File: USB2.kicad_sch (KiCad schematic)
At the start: 0 parts

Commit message: usb work cont
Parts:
- added P1: USB_C_Plug_USB2.0, symbol Connector:USB_C_Plug_USB2.0
- added U2: TUSB2046BIVFR, TUSB2046BIVFR:QFP80P900X900X145-32N, symbol TUSB2046BIVFR:TUSB2046BIVFR
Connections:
- new net: P1.A1 (GND), P1.A12 (GND), P1.B1 (GND), P1.B12 (GND)
- new net: P1.A4 (VBUS), P1.A9 (VBUS), P1.B4 (VBUS), P1.B9 (VBUS)
- new net USB2_HOST2_DM: U2.2 (DM0)
- new net USB2_HOST2_DP: U2.1 (DP0)

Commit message: usb work cont
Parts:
- added C1, C2: 100uF, symbol Device:C_Polarized
- added C3, C4: 0.1uF/16V, symbol Device:C_Polarized
- added C5: 10uF/10V, symbol Device:C_Polarized
- added C6: 22uF/10V, symbol Device:C_Polarized
- added C7: 1uF/10V, symbol Device:C_Polarized
- added P2: USB_C_Plug_USB2.0, symbol Connector:USB_C_Plug_USB2.0
- added R1: 4.7k/1%, symbol Device:R
- added R2: 120K, symbol Device:R
- added U3: TPS2044BDR, TPS2044BDR:SOIC127P600X175-16N, symbol TPS2044BDR:TPS2044BDR
- added U4: ~, symbol raxda:SGM2576YN5G/TR
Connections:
- net GND: now reaches P1.A1 (GND), P1.A12 (GND), P1.B1 (GND), P1.B12 (GND)
- net GND: now also P1.S1 (SHIELD), C1.2, C2.2, C3.2, C4.2, C5.2, C6.2, C7.2, P2.A1 (GND), P2.A12 (GND), P2.B1 (GND), P2.B12 (GND), P2.S1 (SHIELD), R1.2, R2.2, U3.1 (GND), U3.5 (GND__1), U4.2 (GND)
- net at P1.A4 (VBUS), P1.A9 (VBUS), P1.B4 (VBUS)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: now also C2.1, U3.14 (OUT2)
- net at P1.A6 (D+): now also U2.16 (DP2)
- net at P1.A7 (D-): now also U2.15 (DM2)
- net at U2.10 (~OVRCUR1): now also U3.16 (~{OC1})
- net at U2.11 (DM1): now also P2.A7 (D-)
- net at U2.12 (DP1): now also P2.A6 (D+)
- net at U2.13 (~PWRON2): now also U3.4 (~{EN2})
- net at U2.14 (~OVRCUR2): now also U3.13 (~{OC2})
- net at U2.9 (~PWRON1): now also U3.3 (~{EN1})
- new net: C1.1, P2.A4 (VBUS), P2.A9 (VBUS), P2.B4 (VBUS), P2.B9 (VBUS), U3.15 (OUT1)
- new net: C3.1, C4.1, C5.1, C6.1, U3.2 (IN1), U3.6 (IN2), U4.1 (VOUT)
- new net: R1.1, U4.3 (OCB)
- new net Camera_GPIO: R2.1, U4.4 (EN)
- new net VCC5V0_USB: C7.1, U4.5 (IN)
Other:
- moved on the sheet: P1

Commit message: usb work cont
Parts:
- added C8: 10uF/10V, symbol Device:C_Polarized
- added C9: 10uF/X5R, symbol Device:C_Polarized
- added R3: 100K, symbol Device:R
- added R4: 3.9K, symbol Device:R
- added R5: 10K, symbol Device:R
- added U5: ~, symbol raxda:SGM2576YN5G/TR
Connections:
- net GND: now also C8.2, R3.2, R4.2, U5.2 (GND)
- net Switched 3.3v: now reaches U2.26 (~EXTMEM)
- net Switched 3.3v: now also C9.1, U5.1 (VOUT)
- new net: R4.1, U5.3 (OCB)
- new net: R3.1, R5.1, U5.4 (EN)
- new net +1.8v_(Output): R5.2
- new net +3.3v_(Output): C8.1, U5.5 (IN)

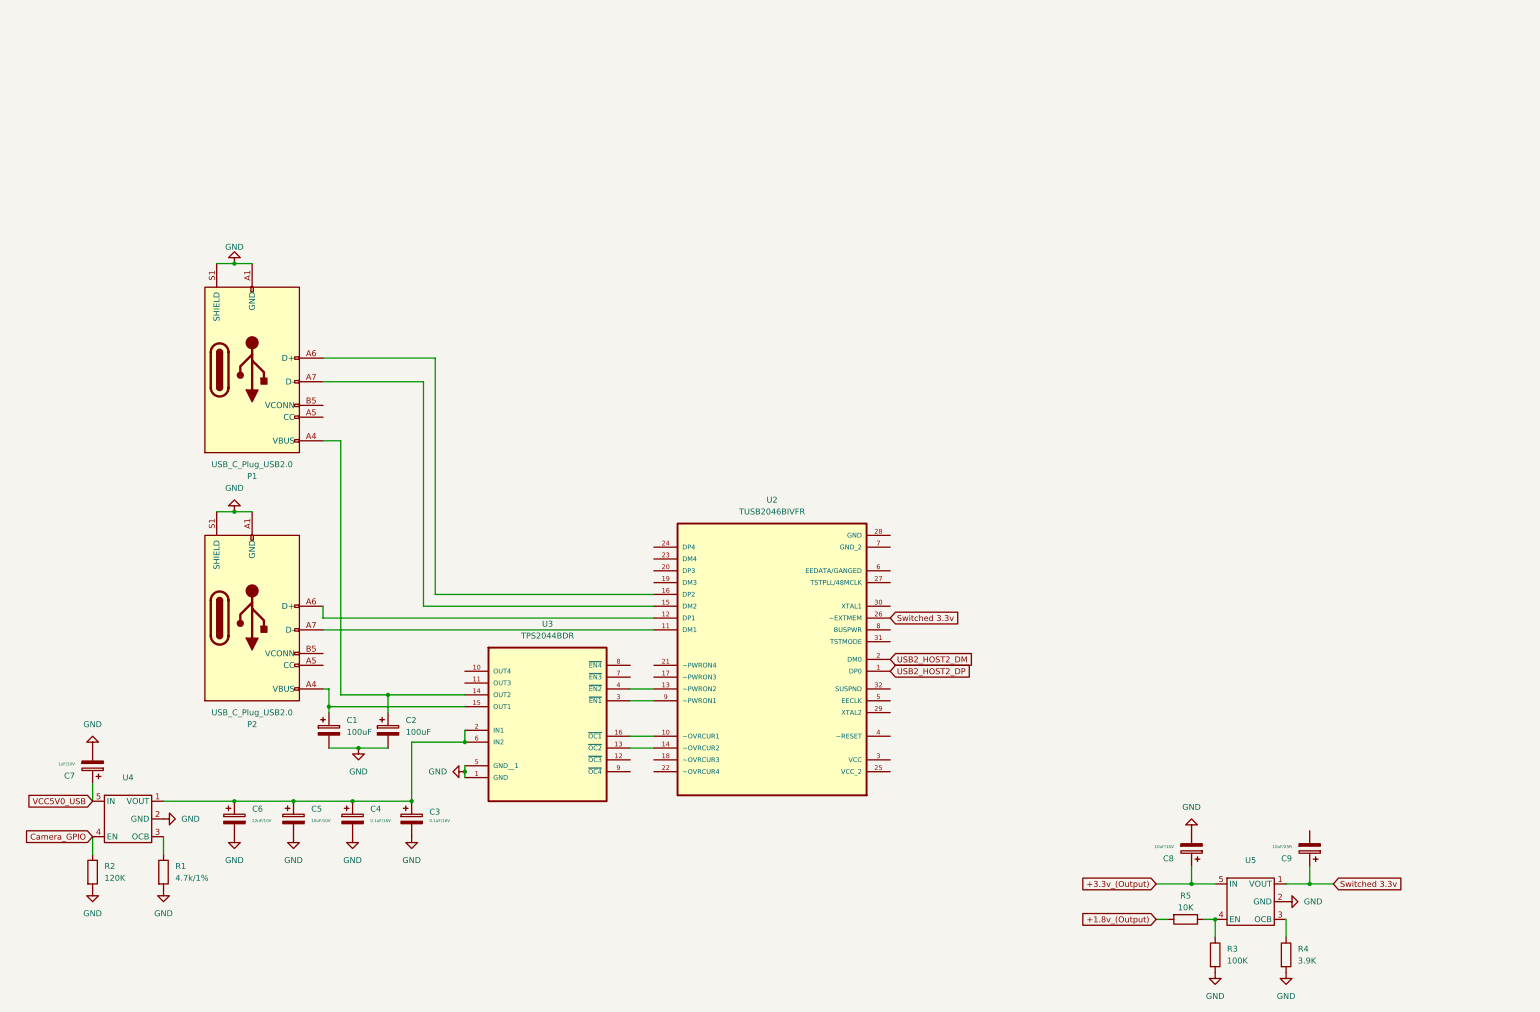
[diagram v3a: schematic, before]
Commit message: finished USB 2.0
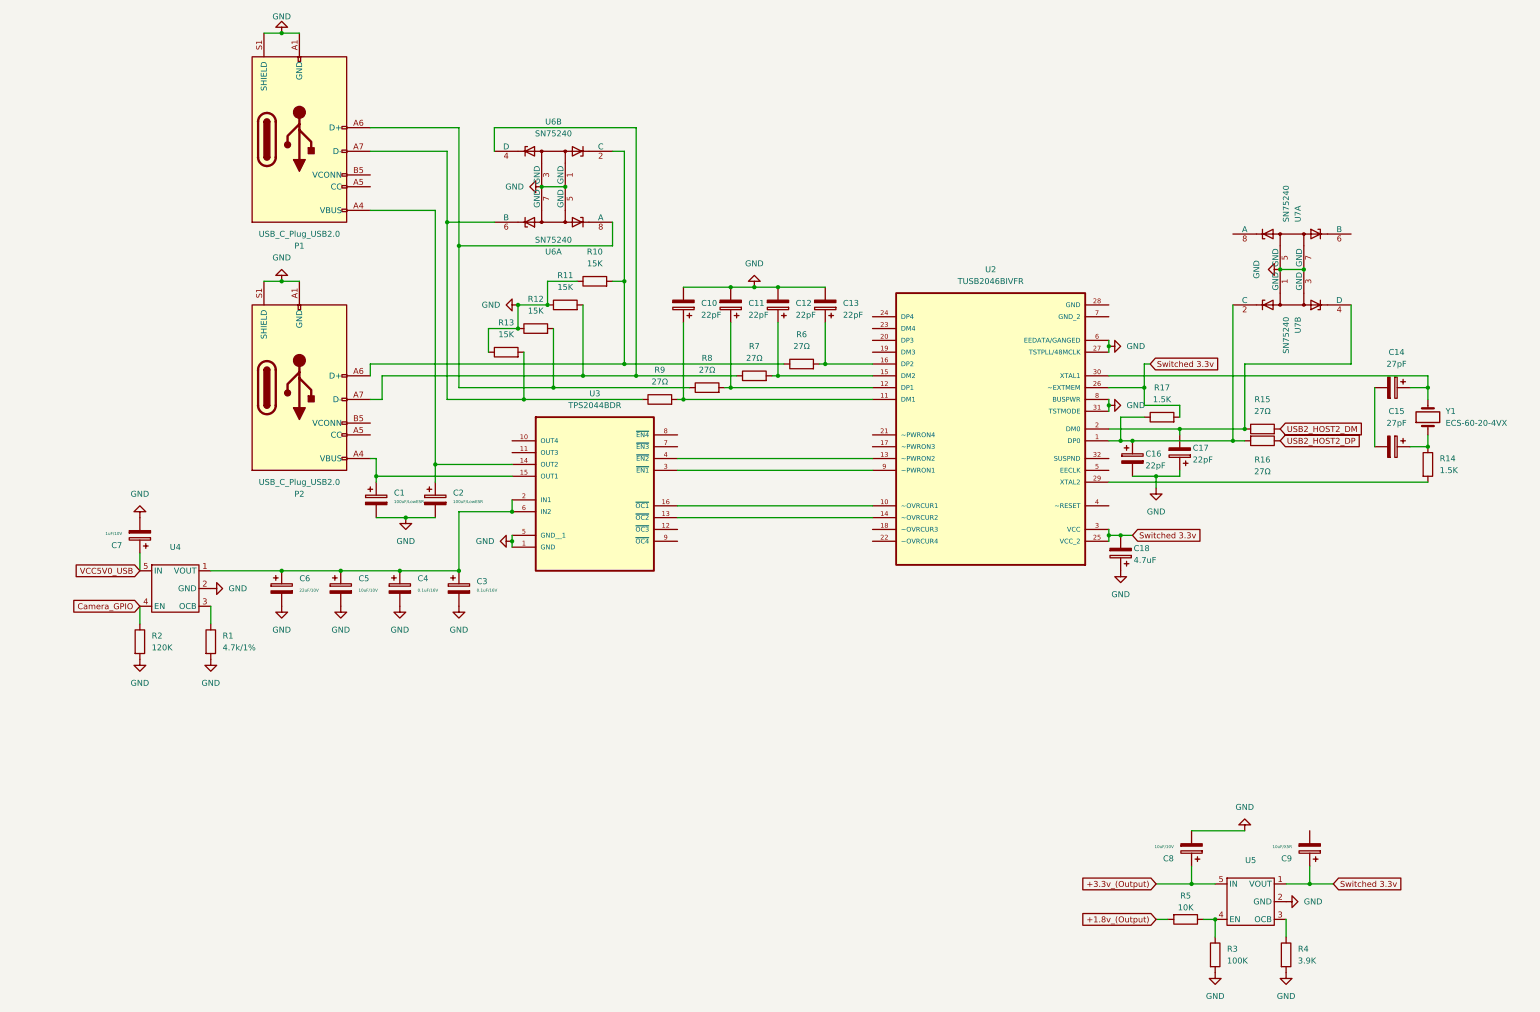
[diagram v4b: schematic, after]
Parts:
- added C10, C11, C12, C13, C16, C17: 22pF, symbol Device:C_Polarized
- added C14, C15: 27pF, symbol Device:C_Polarized
- added C18: 4.7uF, symbol Device:C_Polarized
- added R10, R11, R12, R13: 15K, symbol Device:R
- added R14, R17: 1.5K, symbol Device:R
- added R15, R16, R6, R7, R8, R9: 27Ω, symbol Device:R
- added U6, U7: SN75240, symbol Power_Protection:SN75240
- added Y1: ECS-60-20-4VX, symbol Device:Crystal
- C1, C2: value 100uF -> 100uF/LowESR
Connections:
- net GND: now also U2.27 (TSTPLL/48MCLK), U2.31 (TSTMODE), U2.6 (EEDATA/GANGED), U2.8 (BUSPWR), C10.2, C11.2, C12.2, C13.2, C16.2, C17.1, C18.1, R10.1, R11.1, R12.1, R13.1, U6.1 (GND), U6.3 (GND), U6.5 (GND), U6.7 (GND), U7.1 (GND), U7.3 (GND), U7.5 (GND), U7.7 (GND)
- net Switched 3.3v: now also U2.25 (VCC_2), U2.3 (VCC), C18.2, R17.2
- net USB2_HOST2_DM: now also R15.2; no longer U2.2 (DM0)
- net USB2_HOST2_DP: now also R16.1; no longer U2.1 (DP0)
- net at P1.A6 (D+): now also R12.2, R8.1, U6.8 (A); no longer U2.16 (DP2)
- net at P1.A7 (D-): now also R13.2, R9.1, U6.6 (B); no longer U2.15 (DM2)
- net at U2.11 (DM1): now also C10.1, R9.2; no longer P2.A7 (D-)
- net at U2.12 (DP1): now also C11.1, R8.2; no longer P2.A6 (D+)
- net at U2.29 (XTAL2): now also R14.2
- net at U2.30 (XTAL1): now also C14.1, Y1.2
- new net: C17.2, R15.1, U2.2 (DM0), U7.4 (D)
- new net: P2.A7 (D-), R11.2, R7.1, U6.4 (D)
- new net: C15.1, R14.1, Y1.1
- new net: C14.2, C15.2
- new net: C12.1, R7.2, U2.15 (DM2)
- new net: P2.A6 (D+), R10.2, R6.1, U6.2 (C)
- new net: C13.1, R6.2, U2.16 (DP2)
- new net: C16.1, R16.2, R17.1, U2.1 (DP0), U7.2 (C)
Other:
- moved on the sheet: C1, C2, C3, C4, C5, C6, C7, P1, P2, R1, R2, U2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

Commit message: usb2 fixes and usb3 started
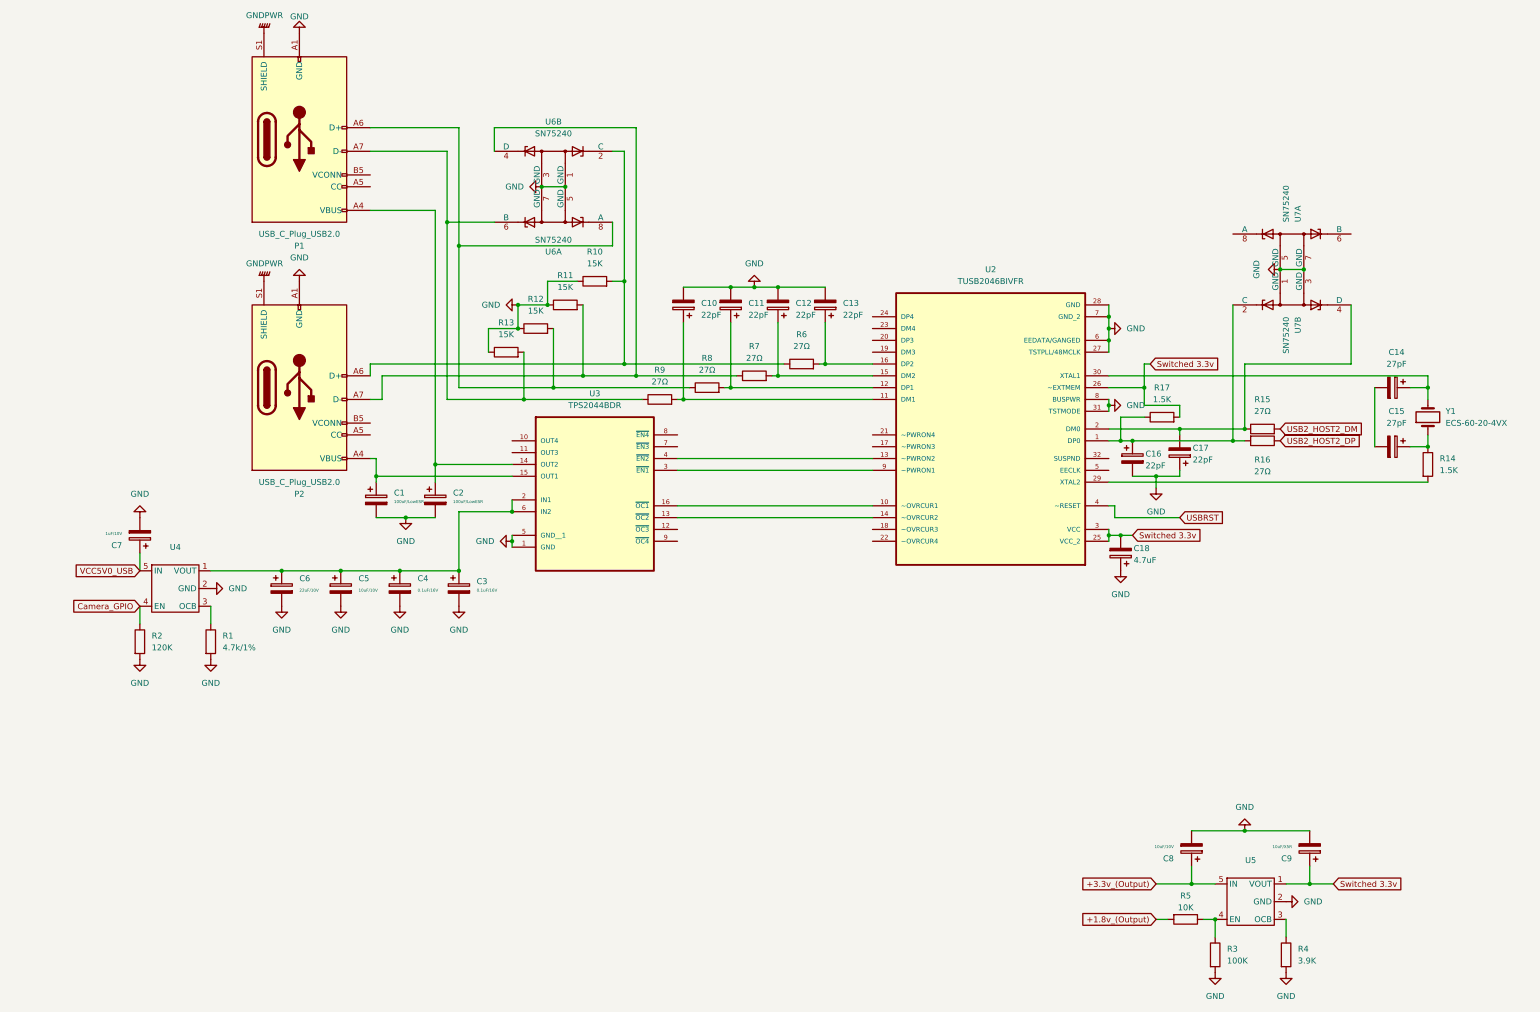
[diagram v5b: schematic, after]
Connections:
- net GND: now also C9.2, U2.28 (GND), U2.7 (GND_2); no longer P1.S1 (SHIELD), P2.S1 (SHIELD)
- net USBRST: now reaches U2.4 (~RESET)
- new net GNDPWR: P1.S1 (SHIELD), P2.S1 (SHIELD)

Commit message: usb3 work cont
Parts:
- Y1: value ECS-60-20-4VX -> MP060
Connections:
- net GND: now also C14.2, C15.2, C17.2; no longer C17.1
- net at R15.1, U2.2 (DM0), U7.4 (D): now also C17.1; no longer C17.2
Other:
- moved on the sheet: C17
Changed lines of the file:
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@@
 	)
 	(junction
+		(at 287.02 128.27)
+		(diameter 0)
+		(color 0 0 0 0)
+	)
+	(junction
 		(at 350.52 116.84)
 		(diameter 0)
@@
 	)
 	(junction
+		(at 292.1 135.89)
+		(diameter 0)
+		(color 0 0 0 0)
+	)
+	(junction
 		(at 130.81 144.78)
 		(diameter 0)
@@
 	)
 	(junction
+		(at 339.09 123.19)
+		(diameter 0)
+		(color 0 0 0 0)
+	)
+	(junction
 		(at 142.24 156.21)
 		(diameter 0)
@@
 	)
 	(junction
-		(at 287.02 128.27)
-		(diameter 0)
-		(color 0 0 0 0)
-	)
-	(junction
 		(at 304.8 231.14)
 		(diameter 0)
@@
 	)
 	(junction
-		(at 292.1 135.89)
-		(diameter 0)
-		(color 0 0 0 0)
-	)
-	(junction
 		(at 210.82 114.3)
 		(diameter 0)
@@
 	(wire
 		(pts
-			(xy 287.02 128.27) (xy 284.48 128.27)
+			(xy 287.02 128.27) (xy 308.61 128.27)
 		)
 		(stroke
@@
 	(wire
 		(pts
-			(xy 339.09 116.84) (xy 339.09 129.54)
+			(xy 339.09 116.84) (xy 339.09 123.19)
 		)
 		(stroke
@@
 	(wire
 		(pts
+			(xy 287.02 135.89) (xy 292.1 135.89)
+		)
+		(stroke
+			(width 0)
+			(type default)
+		)
+	)
+	(wire
+		(pts
 			(xy 156.21 119.38) (xy 181.61 119.38)
 		)
@@
 	(wire
 		(pts
-			(xy 287.02 128.27) (xy 308.61 128.27)
+			(xy 284.48 128.27) (xy 287.02 128.27)
 		)
 		(stroke
@@
 	(wire
 		(pts
-			(xy 287.02 135.89) (xy 292.1 135.89)
-		)
-		(stroke
-			(width 0)
-			(type default)
-		)
-	)
-	(wire
-		(pts
 			(xy 302.26 231.14) (xy 304.8 231.14)
 		)
@@
 	(wire
 		(pts
+			(xy 339.09 123.19) (xy 339.09 129.54)
+		)
+		(stroke
+			(width 0)
+			(type default)
+		)
+	)
+	(wire
+		(pts
 			(xy 311.15 212.09) (xy 299.72 212.09)
 		)
@@
 		)
 	)
-	(global_label "USB2_HOST2_DP"
+	(global_label "+1.8v_(Output)"
 		(shape input)
-		(at 318.77 128.27 0)
+		(at 292.1 231.14 180)
 		(fields_autoplaced yes)
 		(effects
@@
 				(size 1.27 1.27)
 			)
-			(justify left)
+			(justify right)
 		)
 		(property "Intersheetrefs" "${INTERSHEET_REFS}"
-			(at 337.2975 128.27 0)
+			(at 274.6611 231.14 0)
 			(effects
 				(font
 					(size 1.27 1.27)
 				)
-				(justify left)
+				(justify right)
 				(hide yes)
 			)
 		)
 	)
-	(global_label "+1.8v_(Output)"
+	(global_label "Camera_GPIO"
 		(shape input)
-		(at 292.1 231.14 180)
+		(at 73.66 163.83 180)
 		(fields_autoplaced yes)
 		(effects
@@
 		)
 		(property "Intersheetrefs" "${INTERSHEET_REFS}"
-			(at 274.6611 231.14 0)
+			(at 58.0958 163.83 0)
 			(effects
 				(font
@@
 		)
 	)
-	(global_label "Camera_GPIO"
+	(global_label "+3.3v_(Output)"
 		(shape input)
-		(at 73.66 163.83 180)
+		(at 292.1 223.52 180)
 		(fields_autoplaced yes)
 		(effects
@@
 		)
 		(property "Intersheetrefs" "${INTERSHEET_REFS}"
-			(at 58.0958 163.83 0)
+			(at 274.6611 223.52 0)
 			(effects
 				(font
@@
 		)
 	)
-	(global_label "+3.3v_(Output)"
+	(global_label "USB2_HOST2_DP"
 		(shape input)
-		(at 292.1 223.52 180)
+		(at 318.77 128.27 0)
 		(fields_autoplaced yes)
 		(effects
@@
 				(size 1.27 1.27)
 			)
-			(justify right)
+			(justify left)
 		)
 		(property "Intersheetrefs" "${INTERSHEET_REFS}"
-			(at 274.6611 223.52 0)
+			(at 337.2975 128.27 0)
 			(effects
 				(font
 					(size 1.27 1.27)
 				)
-				(justify right)
+				(justify left)
 				(hide yes)
 			)
@@
 			)
 		)
-		(property "Value" "ECS-60-20-4VX"
+		(property "Value" "MP060"
 			(at 354.33 124.4599 90)
 			(effects
@@
 	)
 	(symbol
+		(lib_id "power:GND")
+		(at 339.09 123.19 270)
+		(unit 1)
+		(exclude_from_sim no)
+		(in_bom yes)
+		(on_board yes)
+		(dnp no)
+		(fields_autoplaced yes)
+		(property "Reference" "#PWR035"
+			(at 332.74 123.19 0)
+			(effects
+				(font
+					(size 1.27 1.27)
+				)
+				(hide yes)
+			)
+		)
+		(property "Value" "GND"
+			(at 335.28 123.1899 90)
+			(effects
+				(font
+					(size 1.27 1.27)
+				)
+				(justify right)
+			)
+		)
+		(property "Footprint" ""
+			(at 339.09 123.19 0)
+			(effects
+				(font
+					(size 1.27 1.27)
+				)
+				(hide yes)
+			)
+		)
+		(property "Datasheet" ""
+			(at 339.09 123.19 0)
+			(effects
+				(font
+					(size 1.27 1.27)
+				)
+				(hide yes)
+			)
+		)
+		(property "Description" "Power symbol creates a global label with name \"GND\" , ground"
+			(at 339.09 123.19 0)
+			(effects
+				(font
+					(size 1.27 1.27)
+				)
+				(hide yes)
+			)
+		)
+		(pin "1"
+		)
+		(instances
+			(project ""
+				(path "/600da949-f681-489f-915b-075a1ebe377b/24872095-681f-4aef-afe0-33cd5e3bdeff"
+					(reference "#PWR035")
+					(unit 1)
+				)
+			)
+		)
+	)
+	(symbol
 		(lib_id "Device:R")
 		(at 88.9 171.45 0)
@@
 	(symbol
 		(lib_id "Device:C_Polarized")
-		(at 297.18 130.81 180)
+		(at 297.18 130.81 0)
+		(mirror y)
 		(unit 1)
 		(exclude_from_sim no)
@@
 		(dnp no)
 		(property "Reference" "C17"
-			(at 299.974 129.794 0)
+			(at 299.974 131.826 0)
 			(effects
 				(font
@@
 		)
 		(property "Value" "22pF"
-			(at 299.974 132.334 0)
+			(at 299.974 129.286 0)
 			(effects
 				(font
@@
 		)
 		(property "Footprint" ""
-			(at 296.2148 127 0)
+			(at 296.2148 134.62 0)
 			(effects
 				(font
@@
 		(lib_id "Device:C_Polarized")
 		(at 287.02 132.08 0)
+		(mirror y)
 		(unit 1)
 		(exclude_from_sim no)
@@
 		(dnp no)
 		(property "Reference" "C16"
-			(at 289.814 131.064 0)
+			(at 294.386 130.556 0)
 			(effects
 				(font
@@
 		)
 		(property "Value" "22pF"
-			(at 289.814 133.604 0)
+			(at 294.386 133.096 0)
 			(effects
 				(font
@@
 		)
 		(property "Footprint" ""
-			(at 287.9852 135.89 0)
+			(at 286.0548 135.89 0)
 			(effects
 				(font
